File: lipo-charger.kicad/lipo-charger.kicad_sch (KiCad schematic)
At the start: 20 parts, among them J1 JST-PH2 Device, J2 Alt Device, J3 JST-PH2 Bat, J4 Alt Bat, U1 MCP73831-2-OT, U2 XB6166IS

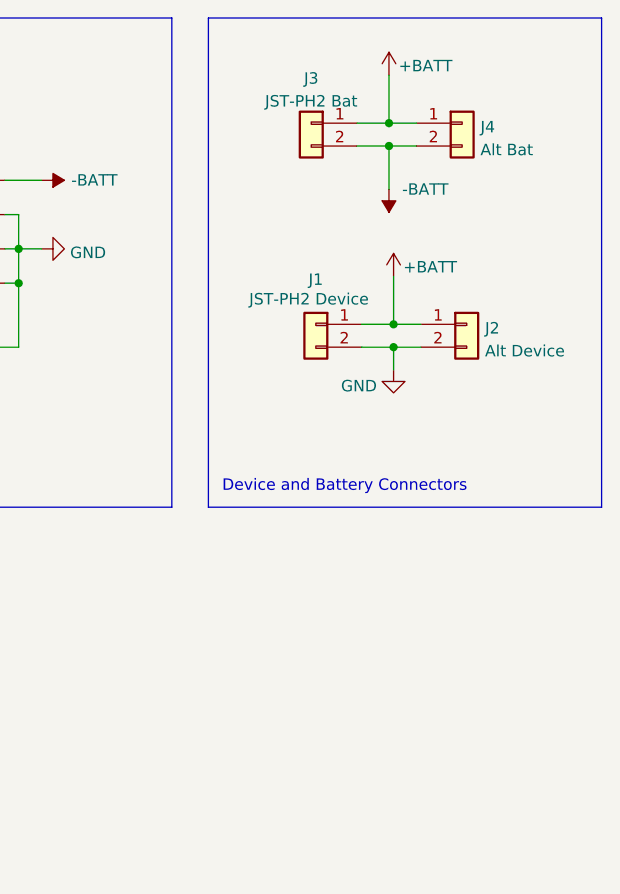
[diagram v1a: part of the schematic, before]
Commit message: Rev: 0.92: add (optional) switch for load
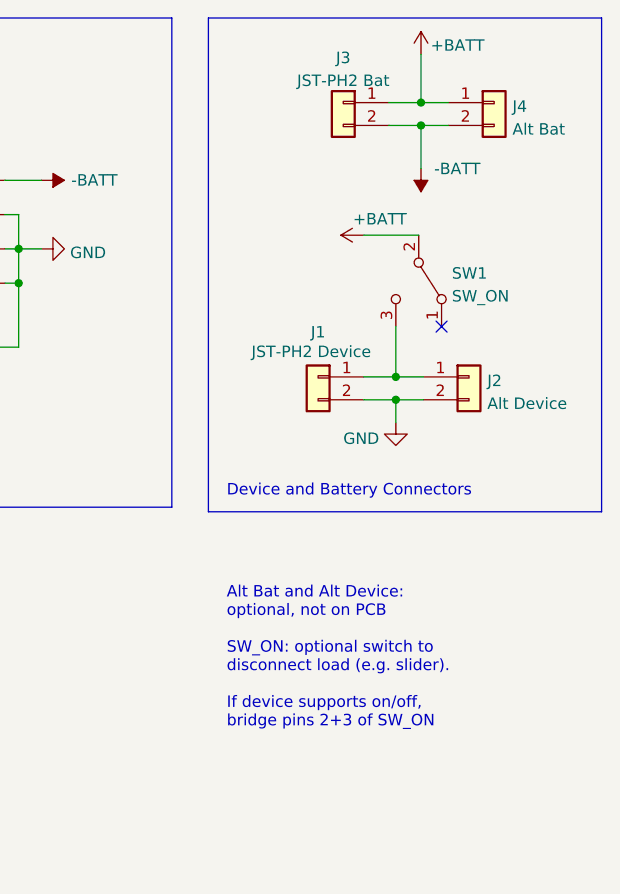
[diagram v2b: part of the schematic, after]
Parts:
- added SW1: SW_ON, Connector_PinHeader_2.54mm:PinHeader_1x03_P2.54mm_Vertical, symbol Switch:SW_SPDT
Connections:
- net +BATT: now also SW1.2 (B); no longer J1.1 (Pin_1), J2.1 (Pin_1)
- new net: J1.1 (Pin_1), J2.1 (Pin_1), SW1.3 (C)
- no-connect marks 3 -> 4
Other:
- note added: "Alt Bat and Alt Device: optional, not on PCB SW_ON: optional switch to disconnect load (e.g. slider). If device supports on/off, bridge pins 2+3 of SW_ON"
- moved on the sheet: J1, J2, J3, J4

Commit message: Rev. 0.93 (added switch for load) - in production
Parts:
- H1, H2, H3, JP1, JP2, SW1: now left out of the parts list
- R3: LCSC C23046 -> C21190
- U1: LCSC C424093 -> C424093
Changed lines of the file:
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@@
   (title_block
     (title "MCP73831/XB6166IS LiPo-Charger")
-    (date "2023-12-30")
-    (rev "0.92")
+    (date "2024-01-02")
+    (rev "0.93")
     (company "Bernhard Bablok")
     (comment 1 "https://github.com/bablokb/pcb-lipo-charger")
@@
   )
   (symbol (lib_id "Jumper:SolderJumper_2_Open") (at 196.596 59.436 0) (unit 1)
-    (in_bom yes) (on_board yes)
+    (in_bom no) (on_board yes)
     (property "Reference" "JP2" (id 0) (at 196.596 57.15 0))
     (property "Value" "No_Protect" (id 1) (at 196.596 62.738 0))
@@
       (effects (font (size 1.27 1.27)) hide)
     )
-    (property "LCSC" " C424093 " (id 4) (at 109.982 50.292 0)
+    (property "LCSC" "C424093" (id 4) (at 109.982 50.292 0)
       (effects (font (size 1.27 1.27)) hide)
     )
@@
   )
   (symbol (lib_id "Jumper:SolderJumper_2_Open") (at 82.55 58.674 0) (unit 1)
-    (in_bom yes) (on_board yes)
+    (in_bom no) (on_board yes)
     (property "Reference" "JP1" (id 0) (at 82.55 56.642 0))
     (property "Value" "Fast_Charge" (id 1) (at 82.55 61.976 0))
@@
   )
   (symbol (lib_id "Mechanical:MountingHole") (at 31.496 176.784 0) (unit 1)
-    (in_bom yes) (on_board yes) (fields_autoplaced)
+    (in_bom no) (on_board yes) (fields_autoplaced)
     (property "Reference" "H2" (id 0) (at 34.036 175.9493 0)
       (effects (font (size 1.27 1.27)) (justify left))
@@
   )
   (symbol (lib_id "Mechanical:MountingHole") (at 56.642 186.944 0) (unit 1)
-    (in_bom yes) (on_board yes) (fields_autoplaced)
+    (in_bom no) (on_board yes) (fields_autoplaced)
     (property "Reference" "H3" (id 0) (at 59.182 186.1093 0)
       (effects (font (size 1.27 1.27)) (justify left))
@@
   )
   (symbol (lib_id "Switch:SW_SPDT") (at 250.444 52.07 270) (unit 1)
-    (in_bom yes) (on_board yes) (fields_autoplaced)
+    (in_bom no) (on_board yes) (fields_autoplaced)
     (property "Reference" "SW1" (id 0) (at 254.127 51.2353 90)
       (effects (font (size 1.27 1.27)) (justify left))
@@
   )
   (symbol (lib_id "Mechanical:MountingHole") (at 56.2516 176.5882 0) (unit 1)
-    (in_bom yes) (on_board yes) (fields_autoplaced)
+    (in_bom no) (on_board yes) (fields_autoplaced)
     (property "Reference" "H1" (id 0) (at 58.7916 175.7535 0)
       (effects (font (size 1.27 1.27)) (justify left))
@@
       (effects (font (size 1.27 1.27)) hide)
     )
-    (property "LCSC" "C23046" (id 4) (at 175.26 44.704 0)
-      (effects (font (size 1.27 1.27)) hide)
-    )
+    (property "LCSC" "C21190" (id 4) (at 175.26 44.704 0)
+      (effects (font (size 1.27 1.27)) hide)
+    )

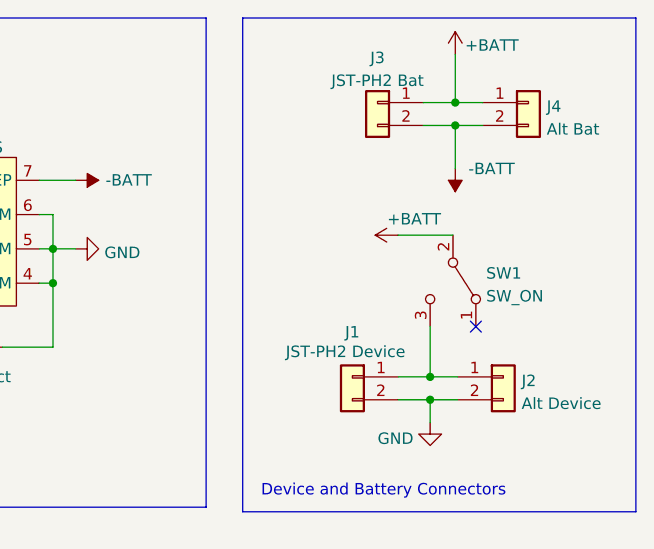
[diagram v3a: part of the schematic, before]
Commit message: Rev 1.10: added 'always-on' trace-jumper
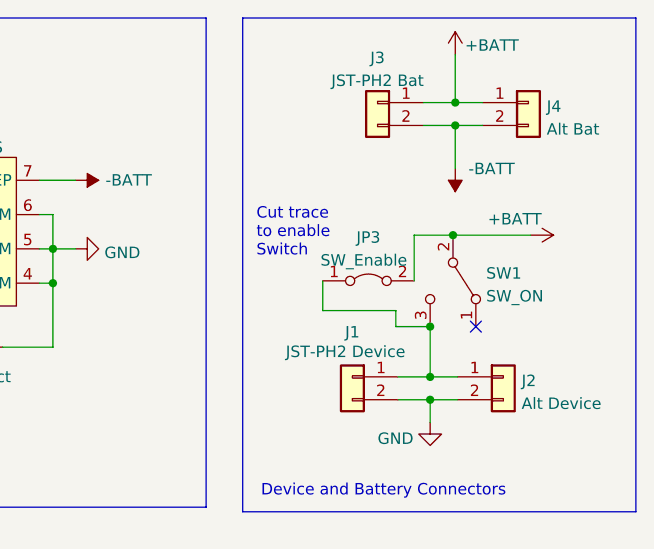
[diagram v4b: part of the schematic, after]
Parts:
- added JP3: SW_Enable, Jumper:SolderJumper-2_P1.3mm_Bridged_Pad1.0x1.5mm, symbol Jumper:Jumper_2_Bridged
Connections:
- net +BATT: now also JP3.2 (B)
- net at J1.1 (Pin_1), J2.1 (Pin_1), SW1.3 (C): now also JP3.1 (A)
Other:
- note added: "Cut trace to enable Switch"
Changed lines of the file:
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@@
   (title_block
     (title "MCP73831/XB6166IS LiPo-Charger")
-    (date "2024-01-02")
-    (rev "0.93")
+    (date "2024-02-01")
+    (rev "1.10")
     (company "Bernhard Bablok")
     (comment 1 "https://github.com/bablokb/pcb-lipo-charger")
@@
   (junction (at 247.904 62.738) (diameter 0) (color 0 0 0 0)
   )
+  (junction (at 247.904 57.15) (diameter 0) (color 0 0 0 0)
+  )
   (junction (at 205.994 52.324) (diameter 0) (color 0 0 0 0)
   )
@@
   )
   (junction (at 186.436 52.324) (diameter 0) (color 0 0 0 0)
+  )
+  (junction (at 250.444 46.99) (diameter 0) (color 0 0 0 0)
   )
   (junction (at 97.536 52.832) (diameter 0) (color 0 0 0 0)
@@
     (stroke (width 0) (type default) (color 0 0 0 0))
   )
+  (wire (pts (xy 246.126 46.99) (xy 250.444 46.99))
+    (stroke (width 0) (type default) (color 0 0 0 0))
+  )
   (polyline (pts (xy 65.278 77.47) (xy 161.036 77.47))
     (stroke (width 0) (type default) (color 0 0 0 0))
@@
     (stroke (width 0) (type default) (color 0 0 0 0))
   )
-  (wire (pts (xy 244.348 46.99) (xy 250.444 46.99))
-    (stroke (width 0) (type default) (color 0 0 0 0))
-  )
   (wire (pts (xy 182.118 52.324) (xy 186.436 52.324))
     (stroke (width 0) (type default) (color 0 0 0 0))
@@
     (stroke (width 0) (type default) (color 0 0 0 0))
   )
+  (wire (pts (xy 247.904 57.15) (xy 244.094 57.15))
+    (stroke (width 0) (type default) (color 0 0 0 0))
+  )
   (wire (pts (xy 87.376 52.832) (xy 75.946 52.832))
     (stroke (width 0) (type default) (color 0 0 0 0))
@@
     (stroke (width 0) (type default) (color 0 0 0 0))
   )
+  (wire (pts (xy 246.126 52.07) (xy 246.126 46.99))
+    (stroke (width 0) (type default) (color 0 0 0 0))
+  )
   (wire (pts (xy 244.348 65.278) (xy 247.904 65.278))
     (stroke (width 0) (type default) (color 0 0 0 0))
@@
     (stroke (width 0) (type default) (color 0 0 0 0))
   )
+  (wire (pts (xy 244.094 55.372) (xy 235.966 55.372))
+    (stroke (width 0) (type default) (color 0 0 0 0))
+  )
   (wire (pts (xy 169.672 44.704) (xy 169.672 40.894))
     (stroke (width 0) (type default) (color 0 0 0 0))
@@
     (stroke (width 0) (type default) (color 0 0 0 0))
   )
+  (wire (pts (xy 235.966 55.372) (xy 235.966 52.07))
+    (stroke (width 0) (type default) (color 0 0 0 0))
+  )
   (wire (pts (xy 205.994 44.704) (xy 205.994 48.514))
     (stroke (width 0) (type default) (color 0 0 0 0))
   )
+  (wire (pts (xy 250.444 46.99) (xy 259.08 46.99))
+    (stroke (width 0) (type default) (color 0 0 0 0))
+  )
   (wire (pts (xy 139.192 52.832) (xy 133.858 52.832))
     (stroke (width 0) (type default) (color 0 0 0 0))
@@
   )
   (wire (pts (xy 54.61 37.592) (xy 54.61 34.29))
+    (stroke (width 0) (type default) (color 0 0 0 0))
+  )
+  (wire (pts (xy 244.094 57.15) (xy 244.094 55.372))
     (stroke (width 0) (type default) (color 0 0 0 0))
   )
@@
     (effects (font (size 1.27 1.27)) (justify left bottom))
   )
+  (text "Cut trace\nto enable\nSwitch" (at 228.6 49.53 0)
+    (effects (font (size 1.27 1.27)) (justify left bottom))
+  )
   (text "MCP73831 Charge IC" (at 66.802 76.454 0)
     (effects (font (size 1.27 1.27)) (justify left bottom))
@@
     (pin "1")
   )
-  (symbol (lib_id "power:+BATT") (at 244.348 46.99 90) (unit 1)
-    (in_bom yes) (on_board yes)
-    (property "Reference" "#PWR04" (id 0) (at 248.158 46.99 0)
-      (effects (font (size 1.27 1.27)) hide)
-    )
-    (property "Value" "+BATT" (id 1) (at 246.126 45.212 90))
-    (property "Footprint" "" (id 2) (at 244.348 46.99 0)
-      (effects (font (size 1.27 1.27)) hide)
-    )
-    (property "Datasheet" "" (id 3) (at 244.348 46.99 0)
+  (symbol (lib_id "power:+BATT") (at 259.08 46.99 270) (mirror x) (unit 1)
+    (in_bom yes) (on_board yes)
+    (property "Reference" "#PWR04" (id 0) (at 255.27 46.99 0)
+      (effects (font (size 1.27 1.27)) hide)
+    )
+    (property "Value" "+BATT" (id 1) (at 257.302 45.212 90))
+    (property "Footprint" "" (id 2) (at 259.08 46.99 0)
+      (effects (font (size 1.27 1.27)) hide)
+    )
+    (property "Datasheet" "" (id 3) (at 259.08 46.99 0)
       (effects (font (size 1.27 1.27)) hide)
     )
@@
     )
   )
+  (symbol (lib_id "Jumper:Jumper_2_Bridged") (at 241.046 52.07 0) (unit 1)
+    (in_bom no) (on_board yes)
+    (property "Reference" "JP3" (id 0) (at 241.046 47.244 0))
+    (property "Value" "SW_Enable" (id 1) (at 240.538 49.784 0))
+    (property "Footprint" "Jumper:SolderJumper-2_P1.3mm_Bridged_Pad1.0x1.5mm" (id 2) (at 241.046 52.07 0)
+      (effects (font (size 1.27 1.27)) hide)
+    )
+    (property "Datasheet" "~" (id 3) (at 241.046 52.07 0)
+      (effects (font (size 1.27 1.27)) hide)
+    )
+    (pin "1")
+    (pin "2")
+  )
   (symbol (lib_id "power:GND") (at 109.982 59.944 0) (unit 1)
     (in_bom yes) (on_board yes) (fields_autoplaced)
@@
       (reference "JP2") (unit 1) (value "No_Protect") (footprint "Jumper:SolderJumper-2_P1.3mm_Open_Pad1.0x1.5mm")
     )
+    (path "/7bc434a3-7c80-42db-87d7-bdc1037cd501"
+      (reference "JP3") (unit 1) (value "SW_Enable") (footprint "Jumper:SolderJumper-2_P1.3mm_Bridged_Pad1.0x1.5mm")
+    )
     (path "/8bf843df-3bbb-4ceb-beef-68f4b9bb61de"
